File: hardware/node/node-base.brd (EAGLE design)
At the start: 83.2 x 53.3 mm, 55 parts, among them IC1 HYPERTRIANGLE_TCS3472FN, Q1 32.768kHz, Q2 24MHz, Q3 BS250, U1 INA322_DGK_8, U2 LMV551_DBV_5, X1 BU-SMA-V

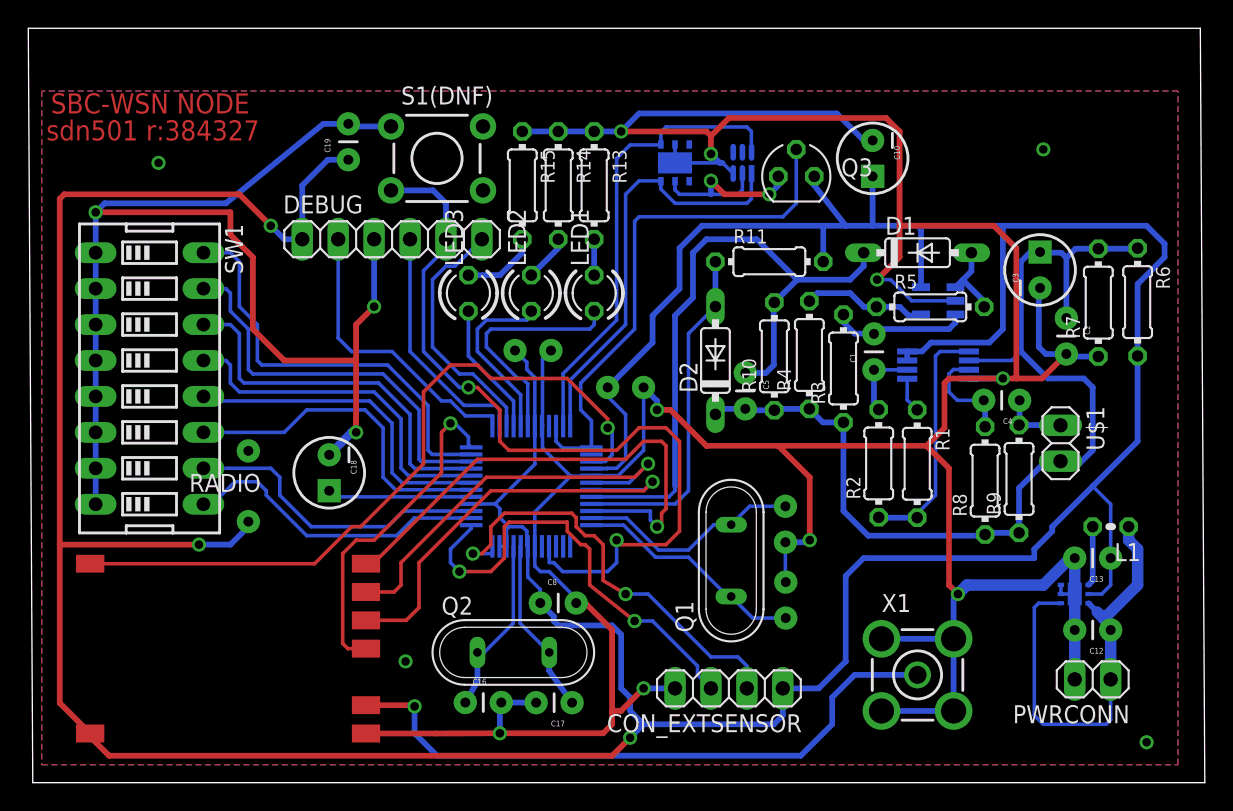
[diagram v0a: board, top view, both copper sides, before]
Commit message: NODEHW: New inductor
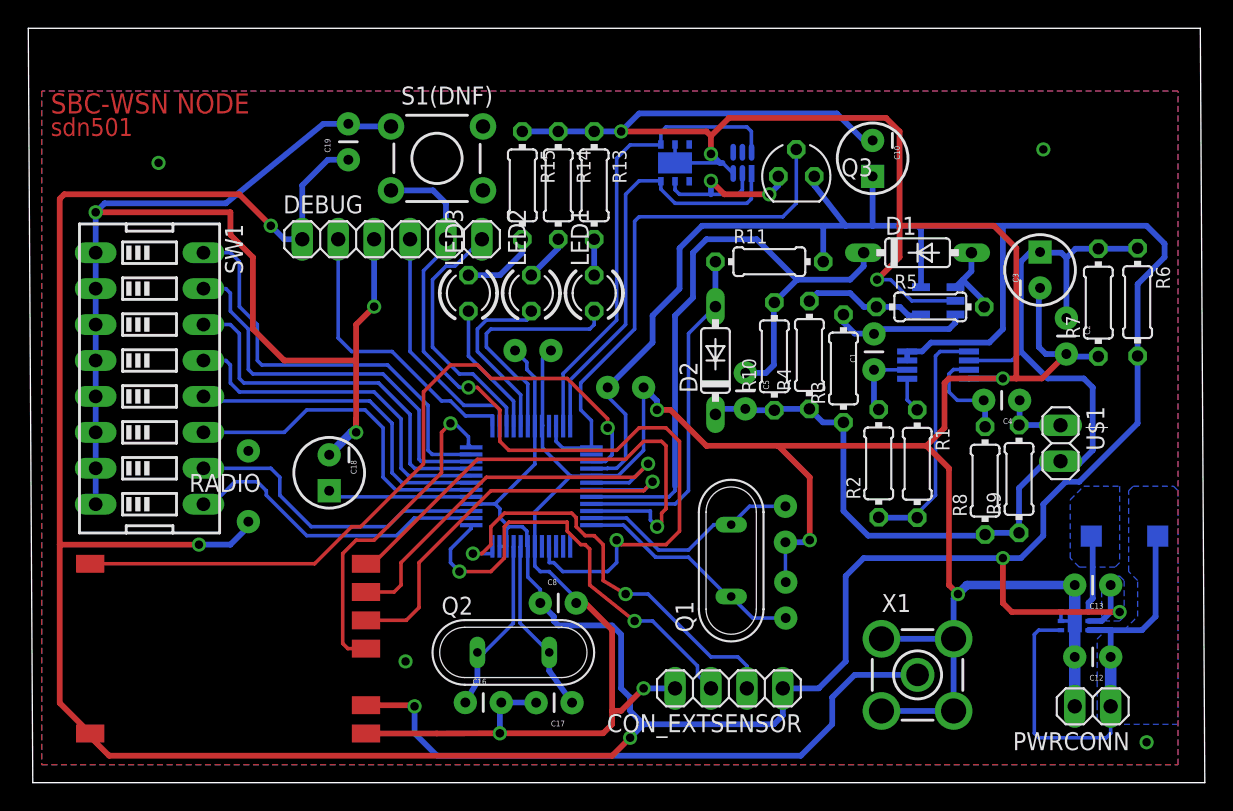
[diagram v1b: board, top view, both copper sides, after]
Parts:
- C12: value 10n -> 10u
- C13: value 10n -> 22u
- L1: value (none) -> 4u7; device resistor:0204V -> FullyCustom:LTF5022
- X1: value BU-SMA-V -> BU-SMA-1-7HOLE; device con-coax:BU-SMA-V -> FullyCustom:SMA_1-7HOLES
- moved U$4 1.91 mm to (73.7, 11.4)
- moved PWRCONN 1.91 mm to (74.9, 5.40)
- moved C12 1.90 mm to (76.2, 8.89)
- moved C13 1.90 mm to (76.2, 14.0)
- moved L1 1.18 mm to (77.2, 17.4), flipped to the bottom, turned to 0 degrees
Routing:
- net +3V3: track 317.4 -> 324.2 mm, vias 3 -> 5
- net GND: track 359.5 -> 357.0 mm
- net VREG_SW: track 4.23 -> 5.52 mm
- net V+: track 33.7 -> 34.7 mm
- added copper zone on layer 16, net V+
- added copper zone on layer 16, net VREG_SW
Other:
- board text added: "sdn501"
- board text removed: "sdn501 r:384327"

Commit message: NODEHW: Changed transistor package, changed caps to SMD
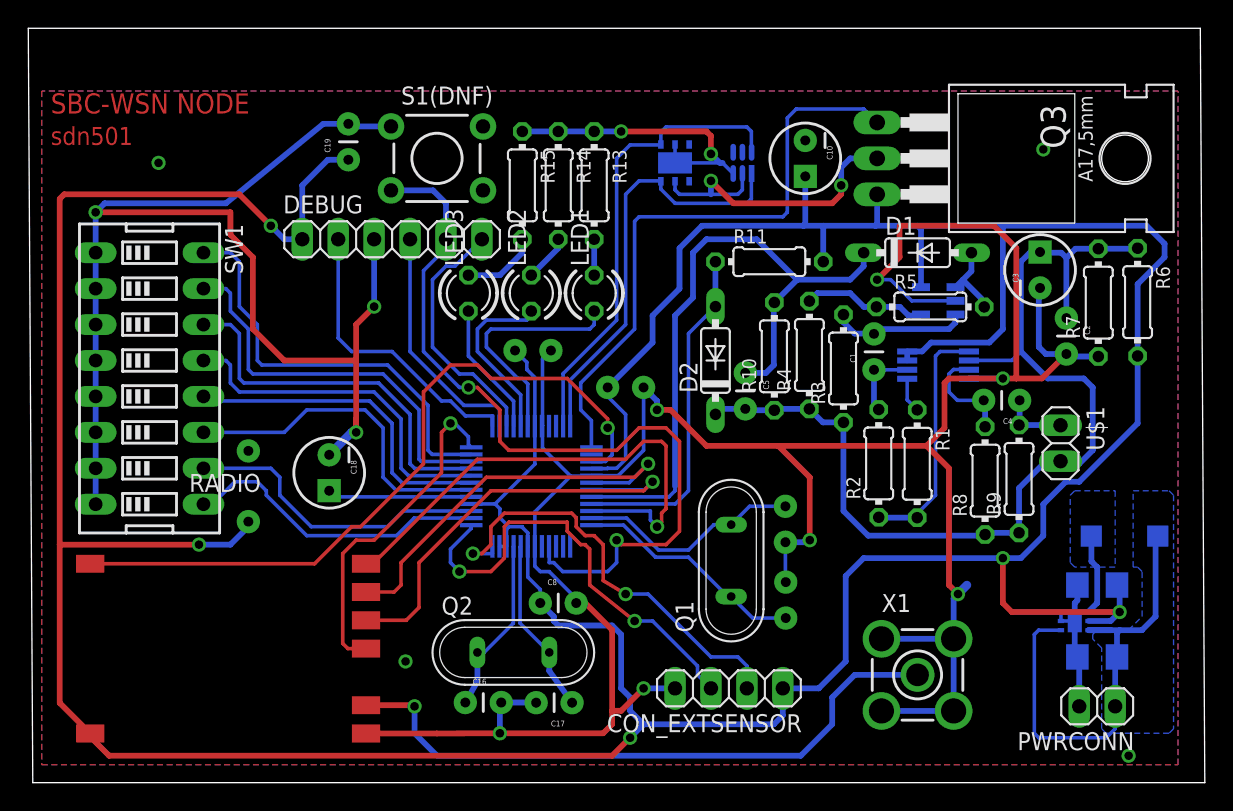
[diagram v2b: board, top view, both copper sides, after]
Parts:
- C12, C13: device SparkFun-Capacitors:CAP-PTH-SMALL -> SparkFun-Capacitors:1206
- Q3: value BS250 -> (none); device transistor-small-signal:SOT54E -> transistor-power:TO220BH
- moved Q3 12.1 mm to (66.0, 44.1), turned to 270 degrees
- moved C10 4.76 mm to (54.6, 44.1)
- moved C12 0.95 mm to (75.2, 8.89), flipped to the bottom, turned to 0 degrees
- moved C13 0.95 mm to (75.2, 14.0), flipped to the bottom, turned to 0 degrees
- moved PWRCONN 0.32 mm to (75.2, 5.40)
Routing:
- net GND: track 357.0 -> 309.5 mm
- net EXT_PWRLINE: track 13.8 -> 22.6 mm
- net EXT_PWRUP: track 37.5 -> 42.6 mm
- net +3V3: track 324.2 -> 322.3 mm
- removed copper zone on layer 16, net +3V3
